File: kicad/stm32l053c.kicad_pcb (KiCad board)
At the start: 2 copper layers, 52 x 35 mm, 43 parts, among them P1 SWD, P2 PWR, Q1 BC807, Q2 BC817, SW1 SW_PUSH, SW2 SW_PUSH, SW3 SW_PUSH, SW4 SW_SPDT, U1 STM32L053C8_LQFP48, U2 TLV61225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

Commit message: Power supply connections
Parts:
- moved SW4 5.16 mm to (165.1, 88.0), turned to 270 degrees
- moved Q2 2.72 mm to (162.2, 94.2)
- moved R6 0.95 mm to (157.3, 96.8)
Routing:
- net Net-(R10-Pad2): track 0.00 -> 13.7 mm
- net Net-(R1-Pad1): track 0.00 -> 13.2 mm
- net Earth: track 58.1 -> 70.2 mm
- net /PNP_BASE: track 0.00 -> 8.64 mm, vias 0 -> 1
- net Net-(Q2-Pad3): track 0.00 -> 7.57 mm
- net Net-(LS1-Pad1): track 0.00 -> 5.95 mm
- net Net-(R9-Pad2): track 0.00 -> 5.05 mm
- net /NPN_BASE: track 0.00 -> 4.93 mm
- net +BATT: track 7.04 -> 9.57 mm
- net /MELODY: track 10.4 -> 12.3 mm
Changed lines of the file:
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@@
   (general
     (links 113)
-    (no_connects 54)
-    (area 116.924999 85.524999 169.075001 120.675001)
+    (no_connects 46)
+    (area 107.214285 78.015 185.166669 135.515001)
     (thickness 1.6)
     (drawings 20)
-    (tracks 326)
+    (tracks 382)
     (zones 0)
     (modules 43)
@@
   )
   (module Resistors_SMD:R_0805_HandSoldering (layer F.Cu)
-    (at 157.25 95.85)
+    (at 157.3 96.8)
     (descr "Resistor SMD 0805, hand soldering")
     (tags "resistor 0805")
@@
   )
   (module TO_SOT_Packages_SMD:SOT-23_Handsoldering (layer F.Cu)
-    (at 163 91.6 270)
+    (at 162.2 94.2 270)
     (descr "SOT-23, Handsoldering")
     (tags SOT-23)
@@
   )
   (module Pin_Headers:Pin_Header_Straight_1x03_Pitch2.54mm (layer F.Cu)
-    (at 160 87.6 90)
+    (at 165.14 88 270)
     (descr "Through hole straight pin header, 1x03, 2.54mm pitch, single row")
     (tags "Through hole pin header THT 1x03 2.54mm single row")
-    (fp_text reference SW4 (at 0 -2.39 90) (layer F.SilkS)
-      (effects (font (size 1 1) (thickness 0.15)))
-    )
-    (fp_text value SW_SPDT (at 0 7.47 90) (layer F.Fab)
+    (fp_text reference SW4 (at 0 -2.39 270) (layer F.SilkS)
+      (effects (font (size 1 1) (thickness 0.15)))
+    )
+    (fp_text value SW_SPDT (at 0 7.47 270) (layer F.Fab)
       (effects (font (size 1 1) (thickness 0.15)))
     )
@@
     (fp_line (start 1.6 6.6) (end 1.6 -1.6) (layer F.CrtYd) (width 0.05))
     (fp_line (start 1.6 -1.6) (end -1.6 -1.6) (layer F.CrtYd) (width 0.05))
-    (pad 1 thru_hole rect (at 0 0 90) (size 1.7 1.7) (drill 1) (layers *.Cu *.Mask)
+    (pad 1 thru_hole rect (at 0 0 270) (size 1.7 1.7) (drill 1) (layers *.Cu *.Mask)
       (net 40 "Net-(R10-Pad2)"))
-    (pad 2 thru_hole oval (at 0 2.54 90) (size 1.7 1.7) (drill 1) (layers *.Cu *.Mask)
+    (pad 2 thru_hole oval (at 0 2.54 270) (size 1.7 1.7) (drill 1) (layers *.Cu *.Mask)
       (net 37 /NPN_BASE))
-    (pad 3 thru_hole oval (at 0 5.08 90) (size 1.7 1.7) (drill 1) (layers *.Cu *.Mask)
+    (pad 3 thru_hole oval (at 0 5.08 270) (size 1.7 1.7) (drill 1) (layers *.Cu *.Mask)
       (net 39 "Net-(R9-Pad2)"))
     (model Pin_Headers.3dshapes/Pin_Header_Straight_1x03_Pitch2.54mm.wrl
@@
   (segment (start 140.95 93.85) (end 139.65 93.85) (width 0.254) (layer F.Cu) (net 1))
   (via (at 141.2 94.1) (size 0.762) (drill 0.4064) (layers F.Cu B.Cu) (net 1))
+  (segment (start 166.5 98.471) (end 166.484001 98.455001) (width 0.254) (layer B.Cu) (net 2))
+  (segment (start 166.484001 98.455001) (end 166.484001 97.155999) (width 0.254) (layer B.Cu) (net 2))
+  (segment (start 166.484001 97.155999) (end 167.5 96.14) (width 0.254) (layer B.Cu) (net 2))
+  (segment (start 161.25 92.7) (end 161.25 93.25) (width 0.254) (layer F.Cu) (net 2))
+  (segment (start 161.25 93.25) (end 162.2 94.2) (width 0.254) (layer F.Cu) (net 2))
+  (segment (start 166.06316 96.14) (end 167.5 96.14) (width 0.254) (layer F.Cu) (net 2))
+  (segment (start 162.2 94.2) (end 163.6 94.2) (width 0.254) (layer F.Cu) (net 2))
+  (segment (start 163.6 94.2) (end 165.54 96.14) (width 0.254) (layer F.Cu) (net 2))
+  (segment (start 165.54 96.14) (end 166.06316 96.14) (width 0.254) (layer F.Cu) (net 2))
+  (segment (start 157.243953 96.901379) (end 155.894233 96.901379) (width 0.254) (layer B.Cu) (net 2))
+  (segment (start 155.894233 96.901379) (end 155.894193 96.901419) (width 0.254) (layer B.Cu) (net 2))
   (segment (start 125.7 90.9) (end 124.06 89.26) (width 0.254) (layer F.Cu) (net 2))
   (segment (start 124.06 89.26) (end 124.06 87.6) (width 0.254) (layer F.Cu) (net 2))
@@
   (segment (start 157.243953 95.732977) (end 157.894193 96.383217) (width 0.254) (layer B.Cu) (net 10))
   (segment (start 157.894193 96.383217) (end 157.894193 96.901379) (width 0.254) (layer B.Cu) (net 10))
+  (segment (start 162.05 94.1) (end 161.5 94.1) (width 0.3556) (layer B.Cu) (net 11))
+  (segment (start 161.5 94.1) (end 160.8 94.8) (width 0.3556) (layer B.Cu) (net 11))
+  (segment (start 160.8 94.8) (end 160.095612 94.8) (width 0.3556) (layer B.Cu) (net 11))
+  (segment (start 160.095612 94.8) (end 159.894193 95.001419) (width 0.3556) (layer B.Cu) (net 11))
   (segment (start 159.895612 91.55) (end 159.494193 91.951419) (width 0.3556) (layer B.Cu) (net 11))
   (segment (start 159.494193 91.951419) (end 159.9 92.357226) (width 0.3556) (layer B.Cu) (net 11))
@@
   (via (at 136.9 95.3) (size 0.762) (drill 0.4064) (layers F.Cu B.Cu) (net 31))
   (segment (start 158.8 102.3) (end 146.75 102.3) (width 0.254) (layer B.Cu) (net 31))
+  (segment (start 155.9 91.85) (end 155.9 93.85) (width 0.254) (layer F.Cu) (net 32))
+  (segment (start 157.3 87.6) (end 157.3 90.55) (width 0.254) (layer F.Cu) (net 32))
+  (segment (start 157.3 90.55) (end 156 91.85) (width 0.254) (layer F.Cu) (net 32))
+  (segment (start 156 91.85) (end 155.9 91.85) (width 0.254) (layer F.Cu) (net 32))
+  (segment (start 152.5 86.75) (end 153.404 86.75) (width 0.254) (layer B.Cu) (net 32))
+  (segment (start 153.404 86.75) (end 153.954 86.2) (width 0.254) (layer B.Cu) (net 32))
+  (segment (start 153.954 86.2) (end 157.1 86.2) (width 0.254) (layer B.Cu) (net 32))
+  (segment (start 157.1 86.2) (end 157.3 86.4) (width 0.254) (layer B.Cu) (net 32))
+  (segment (start 157.3 86.4) (end 157.3 87.6) (width 0.254) (layer B.Cu) (net 32))
   (segment (start 148.4 87.1) (end 150.05 87.1) (width 0.254) (layer B.Cu) (net 33))
   (segment (start 150.05 87.1) (end 152.9 89.95) (width 0.254) (layer B.Cu) (net 33))
@@
   (segment (start 146.496 87.1) (end 148.4 87.1) (width 0.254) (layer F.Cu) (net 33))
   (segment (start 150 94.85) (end 150 93.6) (width 0.254) (layer B.Cu) (net 34))
+  (segment (start 156.07 88.60457) (end 156.07 87.6) (width 0.254) (layer B.Cu) (net 34))
   (segment (start 150 93.6) (end 152 91.6) (width 0.254) (layer B.Cu) (net 34))
-  (segment (start 152 91.6) (end 153 91.6) (width 0.254) (layer B.Cu) (net 34))
-  (segment (start 153 91.6) (end 155.42901 89.17099) (width 0.254) (layer B.Cu) (net 34))
+  (segment (start 152 91.6) (end 153.07457 91.6) (width 0.254) (layer B.Cu) (net 34))
+  (segment (start 153.07457 91.6) (end 156.07 88.60457) (width 0.254) (layer B.Cu) (net 34))
   (segment (start 148.35 95.35) (end 149.5 95.35) (width 0.254) (layer F.Cu) (net 34))
   (via (at 150 94.85) (size 0.762) (drill 0.4064) (layers F.Cu B.Cu) (net 34))
   (segment (start 149.5 95.35) (end 150 94.85) (width 0.254) (layer F.Cu) (net 34))
+  (segment (start 163 91.1) (end 164.25 91.1) (width 0.254) (layer B.Cu) (net 35))
+  (segment (start 167.5 87.85) (end 167.5 87.75) (width 0.254) (layer B.Cu) (net 35))
+  (segment (start 164.25 91.1) (end 167.5 87.85) (width 0.254) (layer B.Cu) (net 35))
+  (segment (start 164 96.5) (end 164 94.15) (width 0.254) (layer B.Cu) (net 36))
+  (segment (start 164 94.15) (end 163.95 94.1) (width 0.254) (layer B.Cu) (net 36))
+  (segment (start 158.65 96.8) (end 158.75 96.8) (width 0.254) (layer F.Cu) (net 36))
+  (segment (start 158.75 96.8) (end 159.654 97.704) (width 0.254) (layer F.Cu) (net 36))
+  (segment (start 159.654 97.704) (end 162.796 97.704) (width 0.254) (layer F.Cu) (net 36))
+  (segment (start 162.796 97.704) (end 164 96.5) (width 0.254) (layer F.Cu) (net 36))
+  (via (at 164 96.5) (size 0.762) (drill 0.4064) (layers F.Cu B.Cu) (net 36))
+  (segment (start 163.15 92.7) (end 163.1 92.65) (width 0.254) (layer F.Cu) (net 37))
+  (segment (start 162.7 90.2) (end 162.7 88.1) (width 0.254) (layer F.Cu) (net 37))
+  (segment (start 163.1 92.65) (end 163.1 90.6) (width 0.254) (layer F.Cu) (net 37))
+  (segment (start 163.1 90.6) (end 162.7 90.2) (width 0.254) (layer F.Cu) (net 37))
+  (segment (start 162.7 88.1) (end 162.6 88) (width 0.254) (layer F.Cu) (net 37))
+  (segment (start 162.2 95.7) (end 161.8 95.3) (width 0.254) (layer F.Cu) (net 38))
+  (segment (start 161.8 95.3) (end 156.546 95.3) (width 0.254) (layer F.Cu) (net 38))
+  (segment (start 156.546 95.3) (end 155.95 95.896) (width 0.254) (layer F.Cu) (net 38))
+  (segment (start 155.95 95.896) (end 155.95 96.8) (width 0.254) (layer F.Cu) (net 38))
+  (segment (start 158.6 91.85) (end 158.6 89.46) (width 0.254) (layer F.Cu) (net 39))
+  (segment (start 158.6 89.46) (end 160.06 88) (width 0.254) (layer F.Cu) (net 39))
+  (segment (start 160 88.2) (end 160 87.6) (width 0.254) (layer F.Cu) (net 39))
+  (segment (start 158.6 93.85) (end 159.604 93.85) (width 0.254) (layer F.Cu) (net 40))
+  (segment (start 161.3 87.1) (end 161.8 86.6) (width 0.254) (layer F.Cu) (net 40))
+  (segment (start 159.604 93.85) (end 160.1 93.354) (width 0.254) (layer F.Cu) (net 40))
+  (segment (start 160.1 93.354) (end 160.1 90.5) (width 0.254) (layer F.Cu) (net 40))
+  (segment (start 165.14 86.896) (end 165.14 88) (width 0.254) (layer F.Cu) (net 40))
+  (segment (start 160.1 90.5) (end 161.3 89.3) (width 0.254) (layer F.Cu) (net 40))
+  (segment (start 161.3 89.3) (end 161.3 87.1) (width 0.254) (layer F.Cu) (net 40))
+  (segment (start 161.8 86.6) (end 164.844 86.6) (width 0.254) (layer F.Cu) (net 40))
+  (segment (start 164.844 86.6) (end 165.14 86.896) (width 0.254) (layer F.Cu) (net 40))
   (segment (start 142.25 96.95) (end 142.25 97.854) (width 0.254) (layer F.Cu) (net 41))
   (segment (start 147.4 103.9) (end 148.1 104.6) (width 0.254) (layer F.Cu) (net 41))

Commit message: All connected & DRC pass
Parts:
- added REF**: TheApiLogoTiny, theapi:TheApiLogoTiny, F.Cu at (132.0, 108.6)
- added REF**: TheApiLogoTiny, theapi:TheApiLogoTiny, F.Cu at (152.0, 108.6)
- added REF**: TheApiLogo, theapi:TheApiLogoSmall, B.Cu at (123.0, 108.6)
- U2: footprint theapi:SC-70-6 -> SC-70-6
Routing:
- net VDD: track 45.7 -> 182.9 mm, vias 4 -> 5
- net Earth: track 70.2 -> 201.9 mm, vias 5 -> 11
- net Net-(R3-Pad2): track 0.00 -> 19.4 mm, vias 0 -> 1
- net Net-(R5-Pad2): track 0.00 -> 19.1 mm, vias 0 -> 1
- net Net-(R4-Pad2): track 0.00 -> 18.5 mm, vias 0 -> 1
- net +BATT: track 9.57 -> 18.3 mm
- net /BUTTON2: track 37.3 -> 41.3 mm
- net /BUTTON0: track 28.7 -> 31.9 mm
- net /BUTTON1: track 25.7 -> 28.9 mm
- net /MELODY: track 12.3 -> 11.6 mm
- added copper zone on B.Cu, net Earth
- added copper zone on F.Cu, net Earth
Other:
- board size 52 x 35 mm -> 52 x 36 mm
- board text added: "January 2017 v1.0"
- board text added: "Peter Clarke"
- board text added: "github.com/theapi/kitchen_timer_stm32"
- board text removed: "github.com/theapi/kitchen_timer_stm32 v1.0"

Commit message: Image of the readout on the pcb
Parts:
- added G***: LOGO, theapi:hero, B.Cu at (149.0, 104.6)

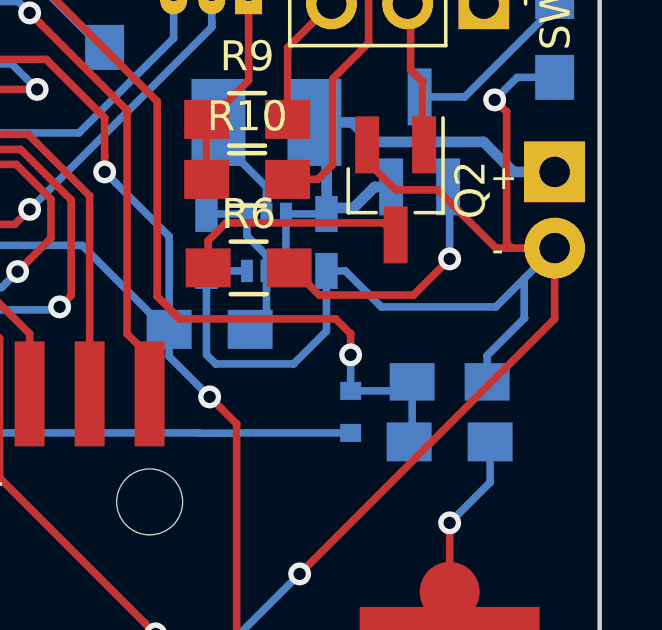
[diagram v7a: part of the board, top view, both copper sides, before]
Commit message: Boost converted on separate ground
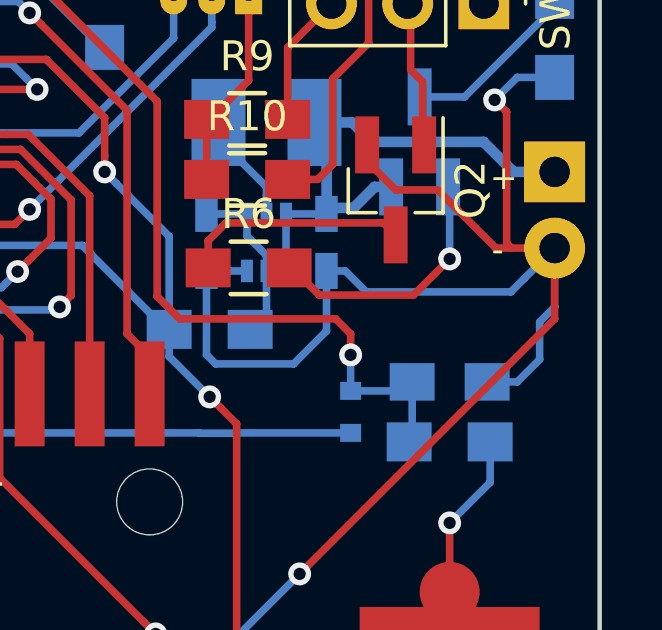
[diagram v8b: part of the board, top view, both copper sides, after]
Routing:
- net Earth: track 201.9 -> 203.5 mm
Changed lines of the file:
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@@
-(kicad_pcb (version 4) (host pcbnew 4.0.5-e0-6337~49~ubuntu16.04.1)
+(kicad_pcb (version 4) (host pcbnew 4.0.2-stable)
   (general
-    (links 0)
+    (links 113)
     (no_connects 0)
-    (area 116.924999 84.524999 169.075001 120.675001)
+    (area 107.139285 79.115 185.241669 135.500001)
     (thickness 1.6)
     (drawings 25)
-    (tracks 555)
+    (tracks 556)
     (zones 0)
     (modules 47)
@@
   (segment (start 140.95 93.85) (end 139.65 93.85) (width 0.254) (layer F.Cu) (net 1))
   (via (at 141.2 94.1) (size 0.762) (drill 0.4064) (layers F.Cu B.Cu) (net 1))
+  (segment (start 159.894193 96.901419) (end 160.523193 96.901419) (width 0.254) (layer B.Cu) (net 2))
+  (segment (start 160.523193 96.901419) (end 161.221774 97.6) (width 0.254) (layer B.Cu) (net 2))
+  (segment (start 161.221774 97.6) (end 166.04 97.6) (width 0.254) (layer B.Cu) (net 2))
+  (segment (start 166.04 97.6) (end 166.484001 97.155999) (width 0.254) (layer B.Cu) (net 2))
+  (segment (start 166.484001 97.155999) (end 167.5 96.14) (width 0.254) (layer B.Cu) (net 2))
+  (segment (start 165.25 100.6) (end 166.254 100.6) (width 0.254) (layer B.Cu) (net 2))
+  (segment (start 167 98.6) (end 167.5 98.1) (width 0.254) (layer B.Cu) (net 2))
+  (segment (start 166.254 100.6) (end 167 99.854) (width 0.254) (layer B.Cu) (net 2))
+  (segment (start 167 99.854) (end 167 98.6) (width 0.254) (layer B.Cu) (net 2))
+  (segment (start 167.5 98.1) (end 167.5 96.14) (width 0.254) (layer B.Cu) (net 2))
   (segment (start 125 93) (end 121.1 93) (width 0.254) (layer F.Cu) (net 2))
   (segment (start 129.65 93) (end 125 93) (width 0.254) (layer F.Cu) (net 2))
@@
   (segment (start 125.4076 86.1) (end 124.06 87.4476) (width 0.254) (layer B.Cu) (net 2))
   (segment (start 124.06 87.4476) (end 124.06 87.6) (width 0.254) (layer B.Cu) (net 2))
-  (segment (start 161.721774 98.1) (end 165.54 98.1) (width 0.254) (layer B.Cu) (net 2))
-  (segment (start 165.54 98.1) (end 166.484001 97.155999) (width 0.254) (layer B.Cu) (net 2))
-  (segment (start 159.894193 96.901419) (end 160.523193 96.901419) (width 0.254) (layer B.Cu) (net 2))
-  (segment (start 160.523193 96.901419) (end 161.721774 98.1) (width 0.254) (layer B.Cu) (net 2))
   (segment (start 137.5 104.6) (end 137.5 103.1) (width 0.254) (layer B.Cu) (net 2))
   (segment (start 137.5 103.1) (end 139.9 100.7) (width 0.254) (layer B.Cu) (net 2))
@@
   (segment (start 147.538815 92.3) (end 147 92.3) (width 0.254) (layer B.Cu) (net 2))
   (segment (start 151.644362 92.3) (end 147.538815 92.3) (width 0.254) (layer B.Cu) (net 2))
-  (segment (start 166.5 98.471) (end 166.484001 98.455001) (width 0.254) (layer B.Cu) (net 2))
-  (segment (start 166.484001 98.455001) (end 166.484001 97.155999) (width 0.254) (layer B.Cu) (net 2))
-  (segment (start 166.484001 97.155999) (end 167.5 96.14) (width 0.254) (layer B.Cu) (net 2))
   (segment (start 161.25 92.7) (end 161.25 93.25) (width 0.254) (layer F.Cu) (net 2))
   (segment (start 161.25 93.25) (end 162.2 94.2) (width 0.254) (layer F.Cu) (net 2))
@@
   (segment (start 134.3 93) (end 134.9 93.6) (width 0.254) (layer F.Cu) (net 2))
   (segment (start 134.9 93.6) (end 137.100002 93.6) (width 0.254) (layer F.Cu) (net 2))
-  (segment (start 165.25 100.6) (end 165.25 99.721) (width 0.254) (layer B.Cu) (net 2))
-  (segment (start 165.25 99.721) (end 166.5 98.471) (width 0.254) (layer B.Cu) (net 2))
   (segment (start 141.5 92.325) (end 141.5 92.000002) (width 0.254) (layer B.Cu) (net 2))
   (segment (start 142.6 93.425) (end 141.5 92.325) (width 0.254) (layer B.Cu) (net 2))
@@
     (polygon
       (pts
-        (xy 155 90.1) (xy 160.5 90.1) (xy 160.5 98.1) (xy 155 98.1)
+        (xy 155 90.1) (xy 160.5 90.1) (xy 160.6 100.5) (xy 155.1 100.5)
       )
     )
@@
       )
     )
+  )
+  (zone (net 0) (net_name "") (layer B.Cu) (hatch edge 0.508)
+    (connect_pads (clearance 0.508))
+    (min_thickness 0.254)
+    (keepout (tracks allowed) (vias allowed) (copperpour not_allowed))
+    (fill (arc_segments 16) (thermal_gap 0.508) (thermal_bridge_width 0.508))
+    (polygon
+      (pts
+        (xy 160.6 96.2) (xy 166.8 96.4) (xy 167.1 97.2) (xy 166 98.5) (xy 160.6 98.5)
+      )
+    )
